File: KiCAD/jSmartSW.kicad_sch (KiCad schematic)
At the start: 22 parts, among them J1 Audio Out, J2 USB4085-GF-A_REVB, J3 EXT, J4 PJ-002A, J5 SBH11-PBPC-D07-RA-BK, J6 Backfeed Power To USBC, P1 To RT4K, P2 From switch output, U1 PICO, U2 SN74LXC1T14DCKR

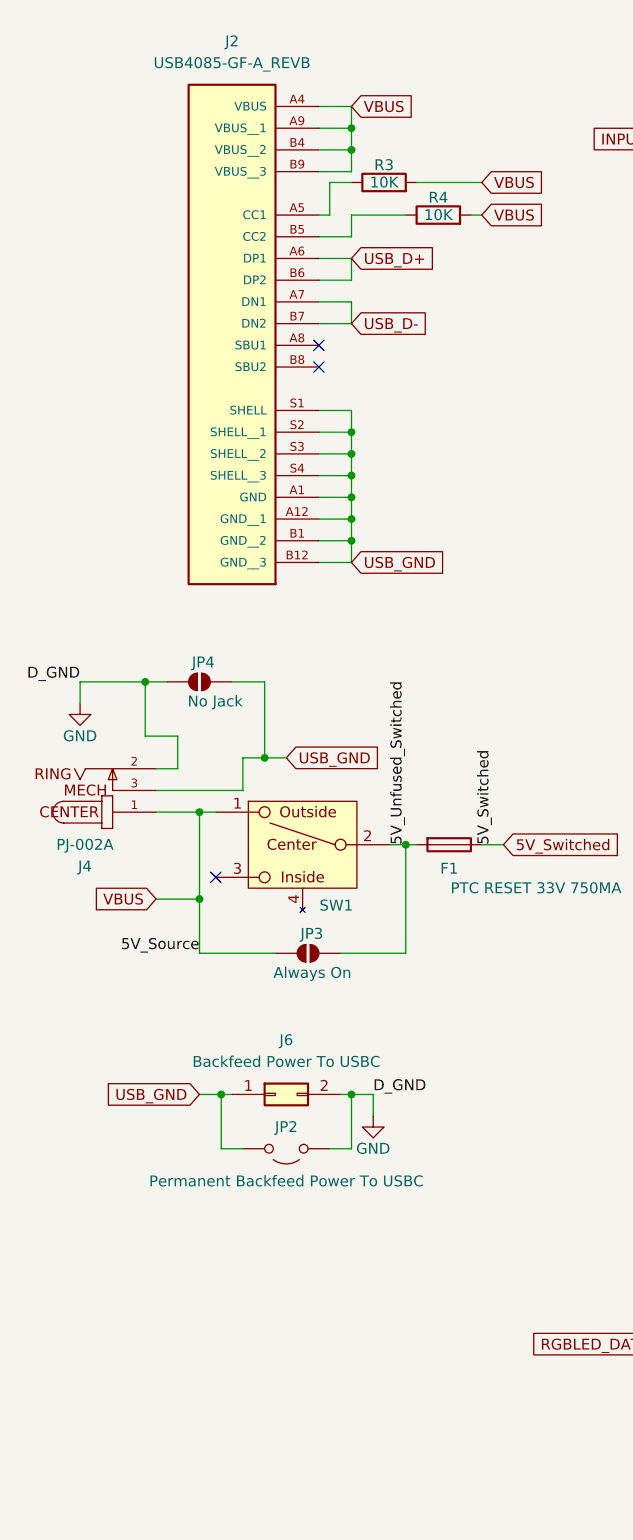
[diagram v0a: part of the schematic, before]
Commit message: Update Main PCB Silkscreen
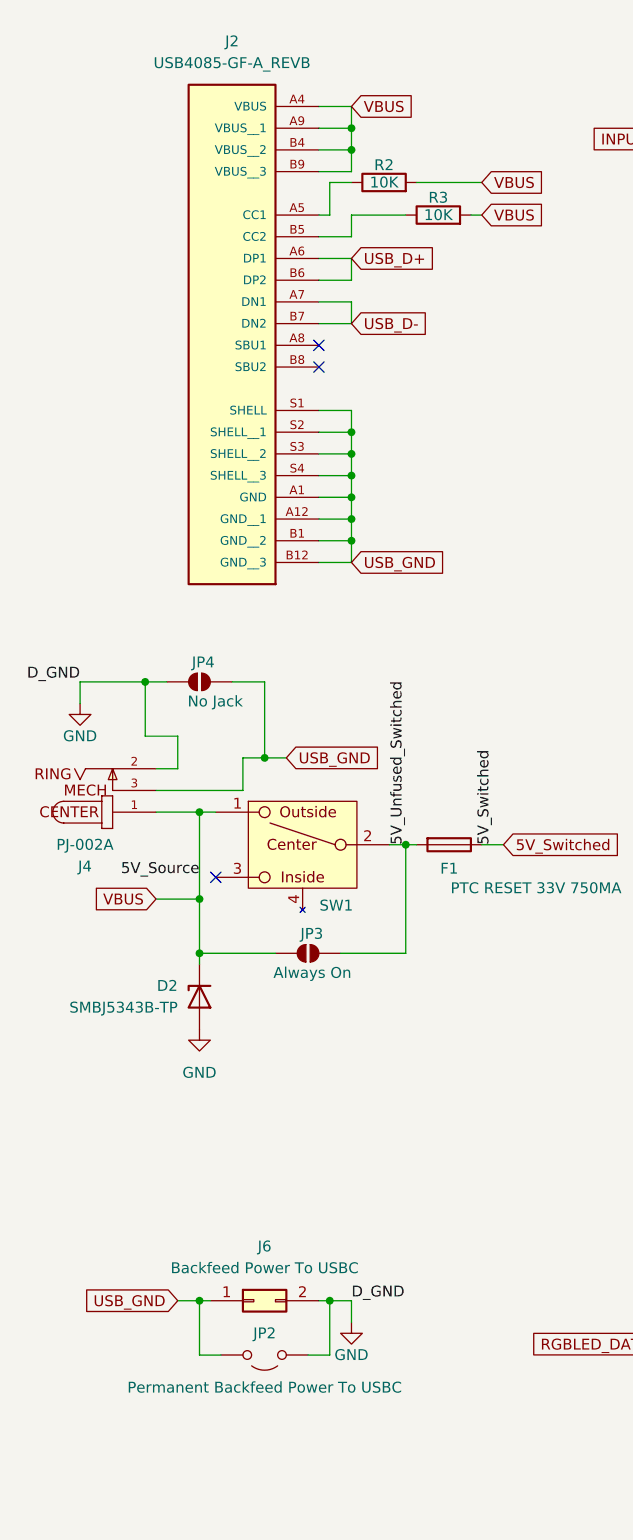
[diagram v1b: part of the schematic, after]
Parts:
- added D2: SMBJ5343B-TP, Diode_SMD:D_SMB, symbol Diode:Z2SMBxxx
- renumbered R3 to R2, R4 to R3
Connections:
- net GND: now also D2.2 (A)
- net VBUS: now also D2.1 (K)
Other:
- moved on the sheet: J6, JP2
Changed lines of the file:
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@@
 	)
 	(junction
+		(at 36.83 129.54)
+		(diameter 0)
+		(color 0 0 0 0)
+	)
+	(junction
 		(at 243.84 111.76)
 		(diameter 0)
@@
 	)
 	(junction
-		(at 39.37 146.05)
+		(at 36.83 170.18)
 		(diameter 0)
 		(color 0 0 0 0)
@@
 	)
 	(junction
-		(at 54.61 146.05)
+		(at 52.07 170.18)
 		(diameter 0)
 		(color 0 0 0 0)
@@
 	(wire
 		(pts
+			(xy 60.96 116.84) (xy 60.96 129.54)
+		)
+		(stroke
+			(width 0)
+			(type default)
+		)
+	)
+	(wire
+		(pts
 			(xy 30.48 97.79) (xy 22.86 97.79)
 		)
@@
 	(wire
 		(pts
-			(xy 39.37 146.05) (xy 40.64 146.05)
+			(xy 36.83 170.18) (xy 38.1 170.18)
 		)
 		(stroke
@@
 	(wire
 		(pts
-			(xy 54.61 152.4) (xy 54.61 146.05)
+			(xy 52.07 176.53) (xy 52.07 170.18)
 		)
 		(stroke
@@
 	(wire
 		(pts
-			(xy 52.07 152.4) (xy 54.61 152.4)
+			(xy 49.53 176.53) (xy 52.07 176.53)
 		)
 		(stroke
@@
 	(wire
 		(pts
+			(xy 36.83 129.54) (xy 36.83 130.81)
+		)
+		(stroke
+			(width 0)
+			(type default)
+		)
+	)
+	(wire
+		(pts
 			(xy 50.8 33.02) (xy 54.61 33.02)
 		)
@@
 	(wire
 		(pts
-			(xy 54.61 146.05) (xy 53.34 146.05)
+			(xy 52.07 170.18) (xy 50.8 170.18)
 		)
 		(stroke
@@
 	(wire
 		(pts
-			(xy 41.91 152.4) (xy 39.37 152.4)
+			(xy 39.37 176.53) (xy 36.83 176.53)
 		)
 		(stroke
@@
 	(wire
 		(pts
-			(xy 57.15 146.05) (xy 54.61 146.05)
+			(xy 54.61 170.18) (xy 52.07 170.18)
 		)
 		(stroke
@@
 	(wire
 		(pts
-			(xy 60.96 129.54) (xy 60.96 116.84)
-		)
-		(stroke
-			(width 0)
-			(type default)
-		)
-	)
-	(wire
-		(pts
 			(xy 36.83 113.03) (xy 38.735 113.03)
 		)
@@
 	(wire
 		(pts
-			(xy 36.83 146.05) (xy 39.37 146.05)
+			(xy 34.29 170.18) (xy 36.83 170.18)
 		)
 		(stroke
@@
 	(wire
 		(pts
-			(xy 57.15 146.05) (xy 57.15 148.59)
+			(xy 54.61 170.18) (xy 54.61 172.72)
 		)
 		(stroke
@@
 	(wire
 		(pts
-			(xy 39.37 152.4) (xy 39.37 146.05)
+			(xy 36.83 176.53) (xy 36.83 170.18)
 		)
 		(stroke
@@
 	)
 	(label "D_GND"
-		(at 57.15 146.05 0)
+		(at 54.61 170.18 0)
 		(effects
 			(font
@@
 	)
 	(label "5V_Source"
-		(at 36.83 129.54 180)
+		(at 36.83 120.65 180)
 		(effects
 			(font
@@
 	(global_label "USB_GND"
 		(shape input)
-		(at 36.83 146.05 180)
+		(at 34.29 170.18 180)
 		(fields_autoplaced yes)
 		(effects
@@
 		)
 		(property "Intersheetrefs" "${INTERSHEET_REFS}"
-			(at 25.1967 146.05 0)
+			(at 22.6567 170.18 0)
 			(effects
 				(font
@@
 		(on_board yes)
 		(dnp no)
-		(property "Reference" "R3"
+		(property "Reference" "R2"
 			(at 58.42 37.338 90)
 			(effects
@@
 			(project ""
 				(path "/e63e39d7-6ac0-4ffd-8aa3-1841a4541b55"
-					(reference "R3")
+					(reference "R2")
 					(unit 1)
 				)
@@
 	)
 	(symbol
+		(lib_id "Diode:Z2SMBxxx")
+		(at 36.83 134.62 90)
+		(mirror x)
+		(unit 1)
+		(exclude_from_sim no)
+		(in_bom yes)
+		(on_board yes)
+		(dnp no)
+		(fields_autoplaced yes)
+		(property "Reference" "D2"
+			(at 34.29 133.3499 90)
+			(effects
+				(font
+					(size 1.27 1.27)
+				)
+				(justify left)
+			)
+		)
+		(property "Value" "SMBJ5343B-TP"
+			(at 34.29 135.8899 90)
+			(effects
+				(font
+					(size 1.27 1.27)
+				)
+				(justify left)
+			)
+		)
+		(property "Footprint" "Diode_SMD:D_SMB"
+			(at 41.275 134.62 0)
+			(effects
+				(font
+					(size 1.27 1.27)
+				)
+				(hide yes)
+			)
+		)
+		(property "Datasheet" "https://diotec.com/tl_files/diotec/files/pdf/datasheets/z2smb1.pdf"
+			(at 36.83 134.62 0)
+			(effects
+				(font
+					(size 1.27 1.27)
+				)
+				(hide yes)
+			)
+		)
+		(property "Description" "2000mW Zener Diode, SMB(DO-214AA)"
+			(at 36.83 134.62 0)
+			(effects
+				(font
+					(size 1.27 1.27)
+				)
+				(hide yes)
+			)
+		)
+		(pin "1"
+		)
+		(pin "2"
+		)
+		(instances
+			(project ""
+				(path "/e63e39d7-6ac0-4ffd-8aa3-1841a4541b55"
+					(reference "D2")
+					(unit 1)
+				)
+			)
+		)
+	)
+	(symbol
 		(lib_id "power:GND")
-		(at 57.15 148.59 0)
+		(at 54.61 172.72 0)
 		(mirror y)
 		(unit 1)
@@
 		(dnp no)
 		(property "Reference" "#PWR02"
-			(at 57.15 154.94 0)
+			(at 54.61 179.07 0)
 			(effects
 				(font
@@
 		)
 		(property "Value" "GND"
-			(at 57.15 152.4 0)
+			(at 54.61 176.53 0)
 			(effects
 				(font
@@
 		)
 		(property "Footprint" ""
-			(at 57.15 148.59 0)
+			(at 54.61 172.72 0)
 			(effects
 				(font
@@
 		)
 		(property "Datasheet" ""
-			(at 57.15 148.59 0)
+			(at 54.61 172.72 0)
 			(effects
 				(font
@@
 		)
 		(property "Description" "Power symbol creates a global label with name \"GND\" , ground"
-			(at 57.15 148.59 0)
+			(at 54.61 172.72 0)
 			(effects
 				(font
@@
 		(on_board yes)
 		(dnp no)
-		(property "Reference" "R4"
+		(property "Reference" "R3"
 			(at 64.77 41.148 90)
 			(effects
@@
 			(project "jSmartSW"
 				(path "/e63e39d7-6ac0-4ffd-8aa3-1841a4541b55"
-					(reference "R4")
+					(reference "R3")
 					(unit 1)
 				)
@@
 	)
 	(symbol
+		(lib_id "power:GND")
+		(at 36.83 138.43 0)
+		(mirror y)
+		(unit 1)
+		(exclude_from_sim no)
+		(in_bom yes)
+		(on_board yes)
+		(dnp no)
+		(fields_autoplaced yes)
+		(property "Reference" "#PWR010"
+			(at 36.83 144.78 0)
+			(effects
+				(font
+					(size 1.27 1.27)
+				)
+				(hide yes)
+			)
+		)
+		(property "Value" "GND"
+			(at 36.83 143.51 0)
+			(effects
+				(font
+					(size 1.27 1.27)
+				)
+			)
+		)
+		(property "Footprint" ""
+			(at 36.83 138.43 0)
+			(effects
+				(font
+					(size 1.27 1.27)
+				)
+				(hide yes)
+			)
+		)
+		(property "Datasheet" ""
+			(at 36.83 138.43 0)
+			(effects
+				(font
+					(size 1.27 1.27)
+				)
+				(hide yes)
+			)
+		)
+		(property "Description" "Power symbol creates a global label with name \"GND\" , ground"
+			(at 36.83 138.43 0)
+			(effects
+				(font
+					(size 1.27 1.27)
+				)
+				(hide yes)
+			)
+		)
+		(pin "1"
+		)
+		(instances
+			(project ""
+				(path "/e63e39d7-6ac0-4ffd-8aa3-1841a4541b55"
+					(reference "#PWR010")
+					(unit 1)
+				)
+			)
+		)
+	)
+	(symbol
 		(lib_id "Jumper:Jumper_2_Open")
-		(at 46.99 152.4 180)
+		(at 44.45 176.53 180)
 		(unit 1)
 		(exclude_from_sim yes)
@@
 		(dnp no)
 		(property "Reference" "JP2"
-			(at 46.99 149.86 0)
+			(at 44.45 173.99 0)
 			(effects
 				(font
@@
 		)
 		(property "Value" "Permanent Backfeed Power To USBC"
-			(at 46.99 156.21 0)
+			(at 44.45 180.34 0)
 			(effects
 				(font
@@
 		)
 		(property "Footprint" "Jumper:SolderJumper-2_P1.3mm_Bridged2Bar_RoundedPad1.0x1.5mm"
-			(at 46.99 152.4 0)
+			(at 44.45 176.53 0)
 			(effects
 				(font
@@
 		)
 		(property "Datasheet" "~"
-			(at 46.99 152.4 0)
+			(at 44.45 176.53 0)
 			(effects
 				(font
@@
 		)
 		(property "Description" "Jumper, 2-pole, open"
-			(at 46.99 152.4 0)
+			(at 44.45 176.53 0)
 			(effects
 				(font
@@
 	(symbol
 		(lib_id "Connector_Generic:Conn_02x01")
-		(at 45.72 146.05 0)
+		(at 43.18 170.18 0)
 		(unit 1)
 		(exclude_from_sim no)
@@
 		(fields_autoplaced yes)
 		(property "Reference" "J6"
-			(at 46.99 139.7 0)
+			(at 44.45 163.83 0)
 			(effects
 				(font
@@
 		)
 		(property "Value" "Backfeed Power To USBC"
-			(at 46.99 142.24 0)
+			(at 44.45 166.37 0)
 			(effects
 				(font
@@
 		)
 		(property "Footprint" "Connector_PinHeader_2.54mm:PinHeader_1x02_P2.54mm_Horizontal"
-			(at 45.72 146.05 0)
+			(at 43.18 170.18 0)
 			(effects
 				(font
@@
 		)
 		(property "Datasheet" "~"
-			(at 45.72 146.05 0)
+			(at 43.18 170.18 0)
 			(effects
 				(font
@@
 		)
 		(property "Description" "Generic connector, double row, 02x01, this symbol is compatible with counter-clockwise, top-bottom and odd-even numbering schemes., script generated (kicad-library-utils/schlib/autogen/connector/)"
-			(at 45.72 146.05 0)
+			(at 43.18 170.18 0)
 			(effects
 				(font
